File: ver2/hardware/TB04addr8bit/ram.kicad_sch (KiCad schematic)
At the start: 5 parts, among them U1 74AHC04, U34 6116, U35 74LS08, U36 74HC00

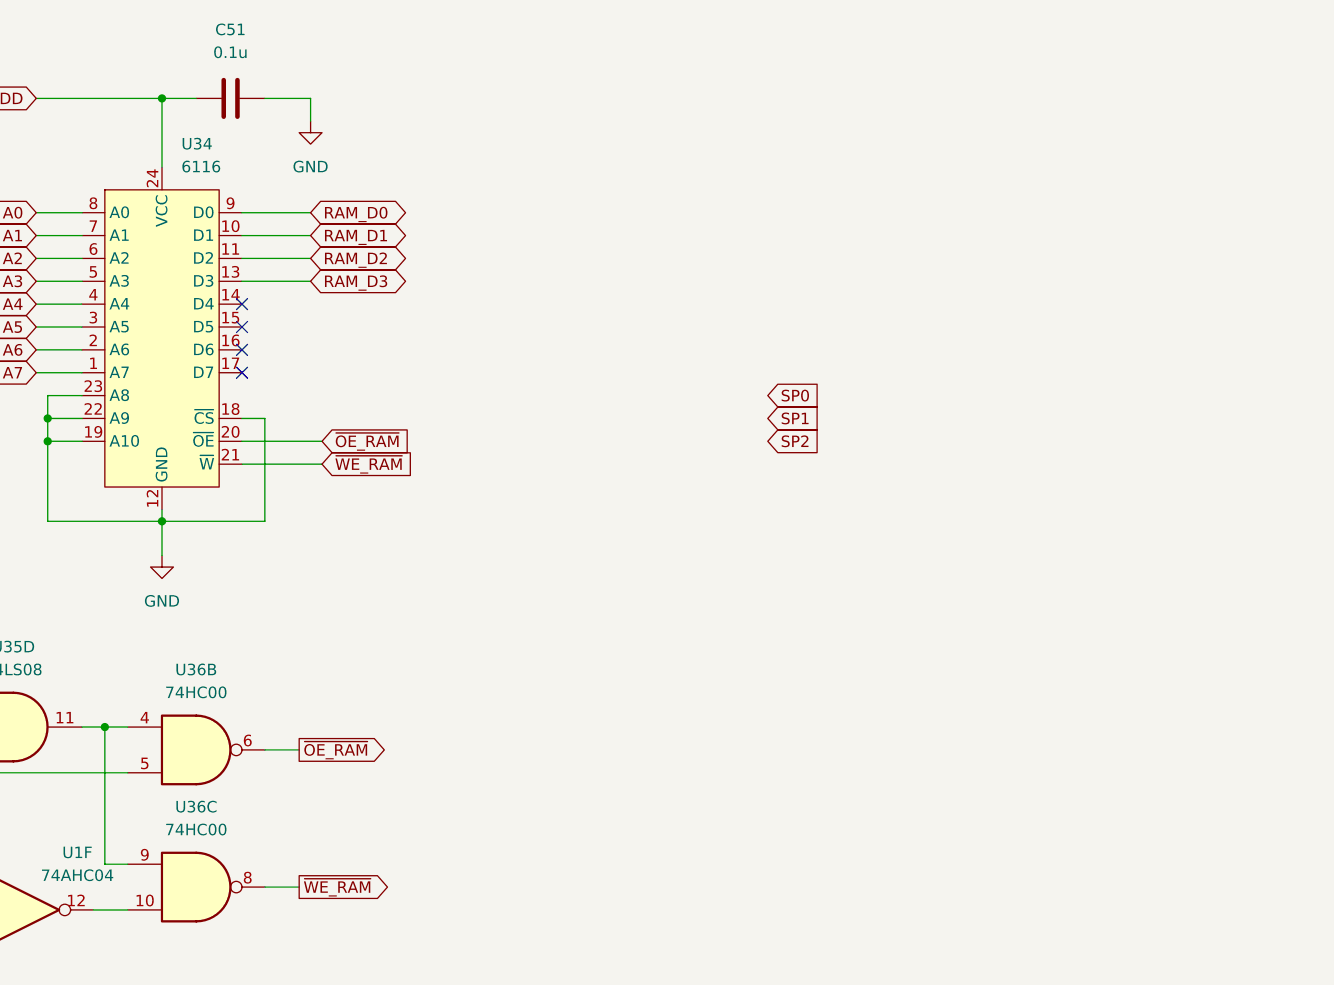
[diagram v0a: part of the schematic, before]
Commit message: ver2: 命令ラッチを1相ずらし、アドレスMUXを完成、I/Oと周辺ICを配置
- 命令ラッチの取り込みエッジを1相ずらし(U20 Cp=FCH1→FCH2 /
  U26 Cp=FCH2→DCR)。EXE中はアドレスバスがmAddrになるため、
  従来はEXE→FCH1の境目でROMのアクセスが間に合わなかった
- /OE_ROM のゲート入力を ~WE から ~WR へ付け替え
  (レジスタ書込許可ではなくメモリ書込で判定するのが正)
- PCの161出力をアドレスバスから切り離し、244経由に変更
  U42(PC)/U43(mAddr)/U44(SP)の入出力を結線し A0-A7 を駆動
  U44は 11110+SP[2:0] で 0xF0-0xF7 を生成。IN/OUT用の244は廃止
- PCのカウントイネーブルを 74LS32 の空きゲートで FCH1|FCH2 として生成
- PC_mAddr シートを PC へ改称し、分岐ロード用の 8bit 2:1 MUX
  (74LS157×2, U14/U15)を新設。出力 PC0-7 を161のD入力へ
  PCカウンタ(IC9/IC10)は addrMUX シートへ移動
- 6116 の /CS にゲートを追加(P2 & !P5)、D4-D7 にラベルを付与
- Yドライバ(74HC244×2, U16/U17)、inPort の 74LS253×2、
  outPort の 74HC273+LED4個 を配置(結線は未)
- ルートから未参照だった ROM_ALU_Decoder / interFace / RS02 を削除

未了: 共通8bitデータバス、オペランド源MUX(SEL_A/SEL_B/SEL_IMM/SEL_Y)、
I/Oポートの結線。PC_mAddr.kicad_sch は PC.kicad_sch と同一内容の
残骸として残っている

Co-Authored-By: Claude Opus 5 <noreply@anthropic.com>
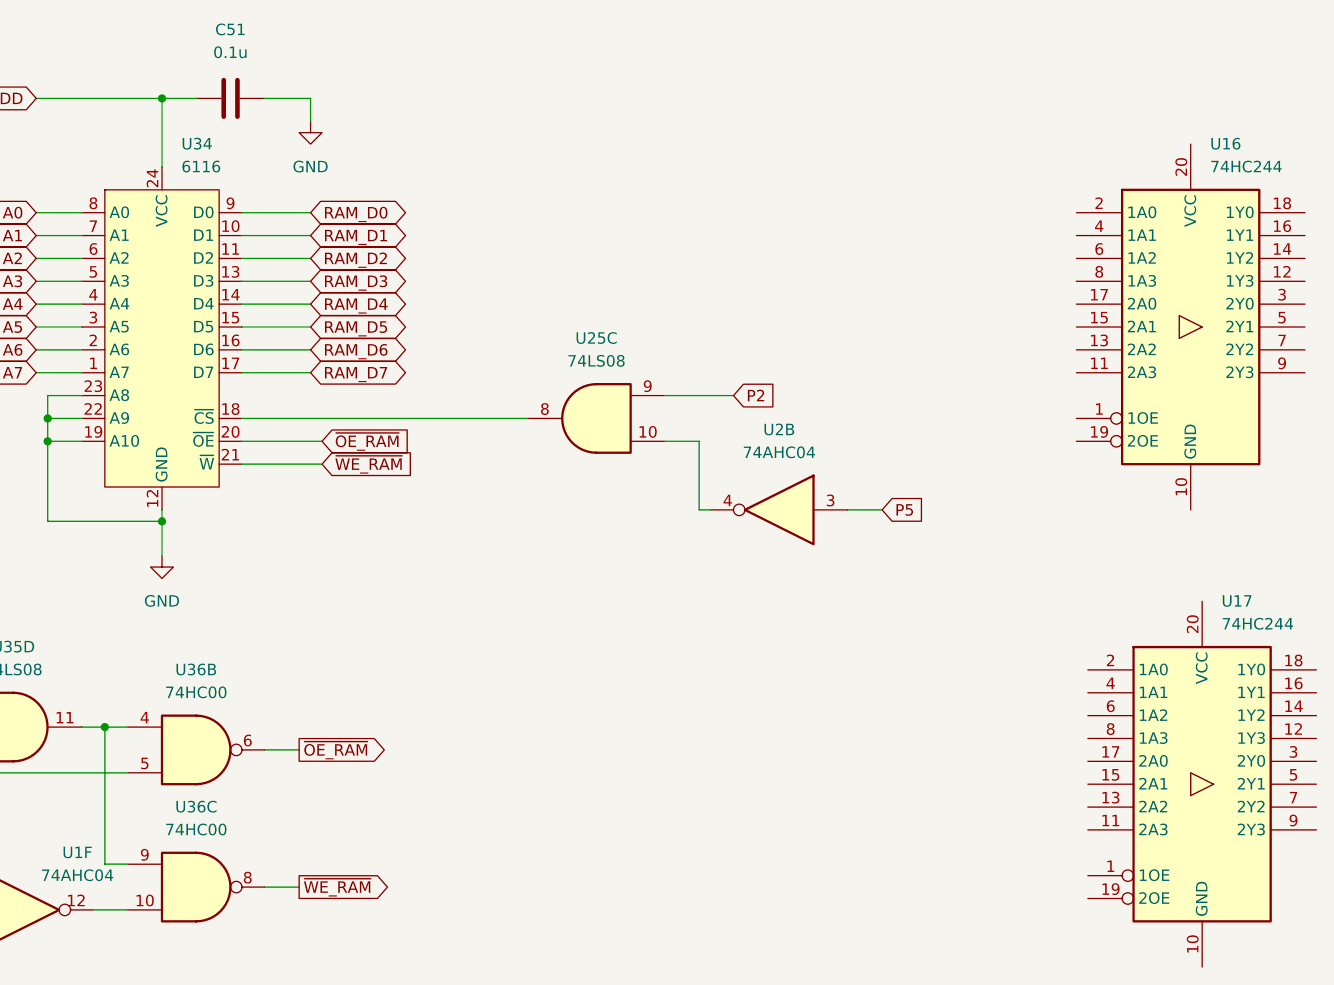
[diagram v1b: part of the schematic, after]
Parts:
- added U16, U17: 74HC244, symbol 74xx:74HC244
- added U2: 74AHC04, symbol 74xx:74AHC04
- added U25: 74LS08, symbol 74xx:74LS08
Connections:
- net GND: no longer U34.18 (~{CS})
- net RAM_D4: now reaches U34.14 (D4)
- net RAM_D5: now reaches U34.15 (D5)
- net RAM_D6: now reaches U34.16 (D6)
- net RAM_D7: now reaches U34.17 (D7)
- new net: U2.4, U25.10
- new net: U25.8, U34.18 (~{CS})
- new net P2: U25.9
- new net P5: U2.3
- no-connect marks 4 -> 0

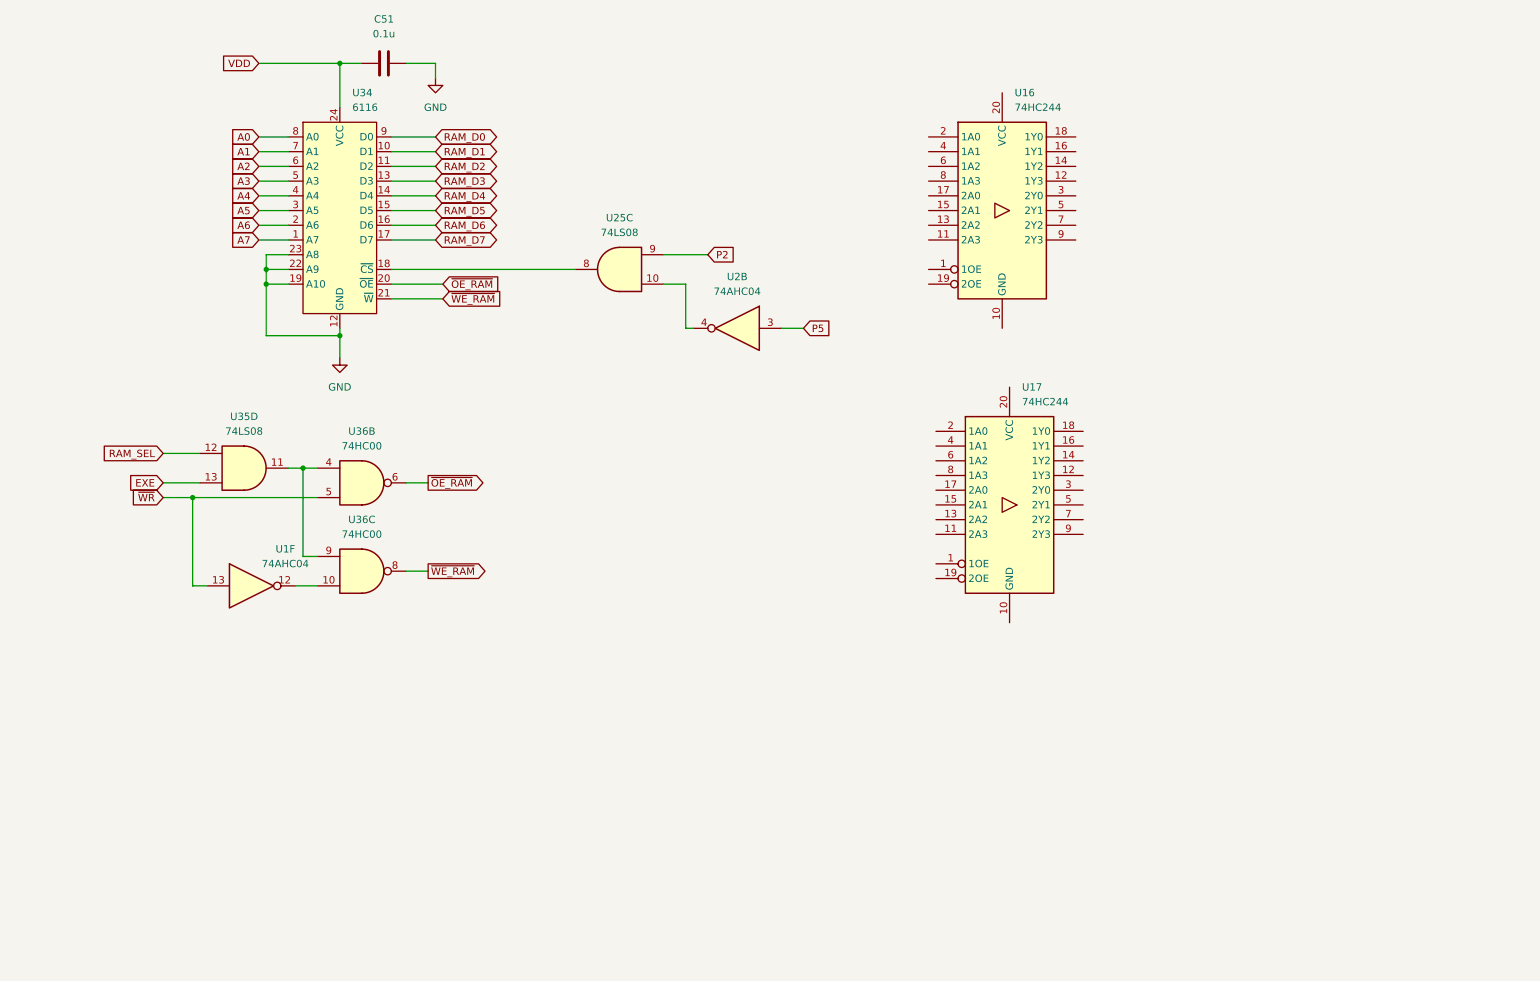
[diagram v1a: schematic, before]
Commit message: ver2: 要修正5件を修正し共通データバス・オペランド源MUX・I/Oを結線
- 6116の/CS極性を修正し、スタック域を含むRAM_STK_SEL(0xC0-0xF7)に統一
- ALU出力をDI0-3へ直結、U21はYドライバ源として残す(LD/POP/RET対策)
- 共通8bitデータバスMD0-7を新設(ROM/RAM/Yドライバ/IN244が排他駆動)
- aポートMUX(74LS253x2)・IN用244・Yドライバ制御ゲートを追加
- IN実行時のROM競合を/OE_ROMに~OE_iAddrを足して回避
- 4bit書込時にMD4-7が浮くのをU17 bank2で0駆動
- 74LS157のEをGND固定、孤立したPC_mAddrシートを削除

Co-Authored-By: Claude Opus 5 <noreply@anthropic.com>
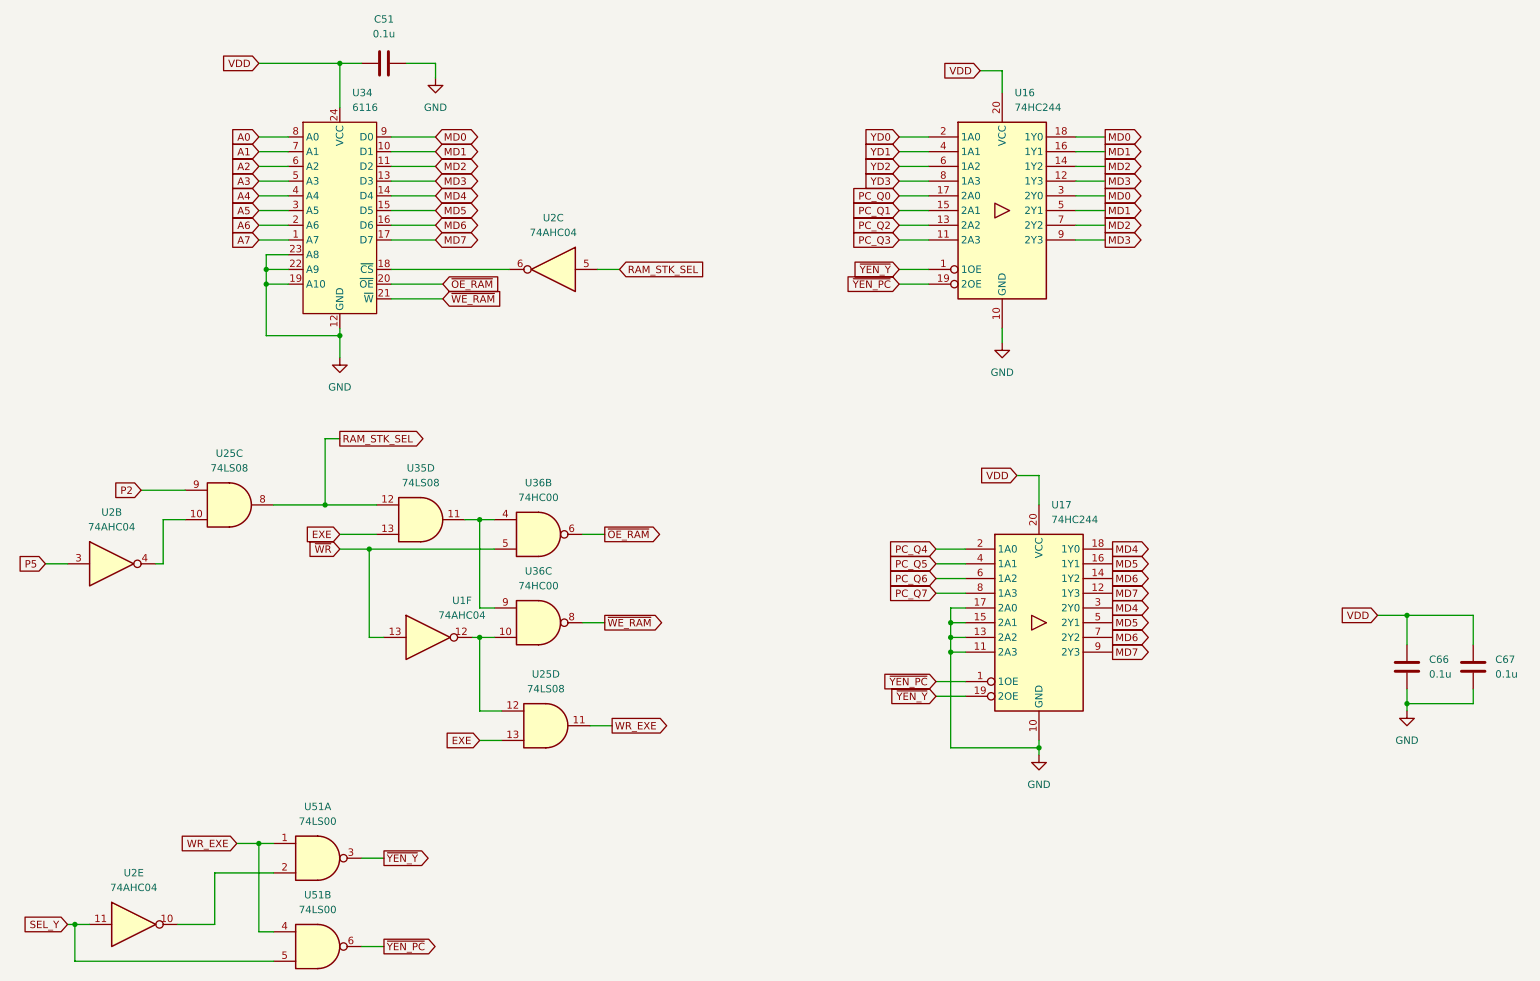
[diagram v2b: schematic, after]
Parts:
- added C66, C67: 0.1u, symbol Device:C
- added unit 3 of U2
- added unit 5 of U2
- added unit 4 of U25
- added U51: 74LS00, symbol 74xx:74LS00
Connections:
- net RAM_D0 is gone; now on net MD0: U34.9 (D0)
- net RAM_D1 is gone; now on net MD1: U34.10 (D1)
- net RAM_D2 is gone; now on net MD2: U34.11 (D2)
- net RAM_D3 is gone; now on net MD3: U34.13 (D3)
- net RAM_D4 is gone; now on net MD4: U34.14 (D4)
- net RAM_D5 is gone; now on net MD5: U34.15 (D5)
- net RAM_D6 is gone; now on net MD6: U34.16 (D6)
- net RAM_D7 is gone; now on net MD7: U34.17 (D7)
- net EXE: now also U25.13
- net GND: now also U16.10 (GND), U17.10 (GND), U17.11 (2A3), U17.13 (2A2), U17.15 (2A1), U17.17 (2A0), C66.1, C67.1
- net VDD: now also U16.20 (VCC), U17.20 (VCC), C66.2, C67.2
- net at U34.18 (~{CS}): now also U2.6; no longer U25.8
- net ~{YEN_PC}: now reaches U17.1 (1OE)
- net ~{YEN_PC}: now also U16.19 (2OE), U51.6
- net MD7: now reaches U17.12 (1Y3)
- net MD7: now also U17.9 (2Y3)
- net MD6: now reaches U17.14 (1Y2)
- net MD6: now also U17.7 (2Y2)
- net MD5: now reaches U17.16 (1Y1)
- net MD5: now also U17.5 (2Y1)
- net MD4: now reaches U17.18 (1Y0)
- net MD4: now also U17.3 (2Y0)
- net ~{YEN_Y}: now reaches U17.19 (2OE)
- net ~{YEN_Y}: now also U16.1 (1OE), U51.3
- net PC_Q4: now reaches U17.2 (1A0)
- net PC_Q5: now reaches U17.4 (1A1)
- net PC_Q6: now reaches U17.6 (1A2)
- net PC_Q7: now reaches U17.8 (1A3)
- net at U1.12, U36.10: now also U25.12
- net PC_Q3: now reaches U16.11 (2A3)
- net MD3: now reaches U16.12 (1Y3)
- net MD3: now also U16.9 (2Y3)
- net PC_Q2: now reaches U16.13 (2A2)
- net MD2: now reaches U16.14 (1Y2)
- net MD2: now also U16.7 (2Y2)
- net PC_Q1: now reaches U16.15 (2A1)
- net MD1: now reaches U16.16 (1Y1)
- net MD1: now also U16.5 (2Y1)
- net PC_Q0: now reaches U16.17 (2A0)
- net MD0: now reaches U16.18 (1Y0)
- net MD0: now also U16.3 (2Y0)
- net YD0: now reaches U16.2 (1A0)
- net YD1: now reaches U16.4 (1A1)
- net YD2: now reaches U16.6 (1A2)
- net YD3: now reaches U16.8 (1A3)
- net RAM_SEL renamed RAM_STK_SEL
- net RAM_STK_SEL: now also U25.8, U2.5
- new net: U2.10, U51.2
- new net SEL_Y: U2.11, U51.5
- new net WR_EXE: U25.11, U51.1, U51.4
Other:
- moved on the sheet: U17, U1F, U2B, U35D, U36B, U36C

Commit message: ver2: ゲートICをgatesシートへ集約しアノテーションを掛け直し
- 分散していた8パッケージ(U1/U2/U5/U25/U35/U36/U37/U51)をgatesシートへ集約
- シートをまたぐ11本をグローバルラベル化(~P4/~P5/~OUT_SEL/~CS_RAM/
  ~OE_ROM/CLK_C/CLK_Z/PC_CNT_EN/~PC_PE/~Ena_RS01/~Enb_RS01)
- U40のP2入力がROM_SELに吸着していたのを修正(RAM_SELが逆条件だった)
- !P5の重複インバータを解消、未使用ゲート入力7本をGNDへ
- ALU入力MUXをinPut→PC、PCカウンタをaddrMUX→PCへ移動
- 全体を再アノテーション(シート順採番)。旧→新の対応は電気的変化なしを確認

Co-Authored-By: Claude Opus 5 <noreply@anthropic.com>
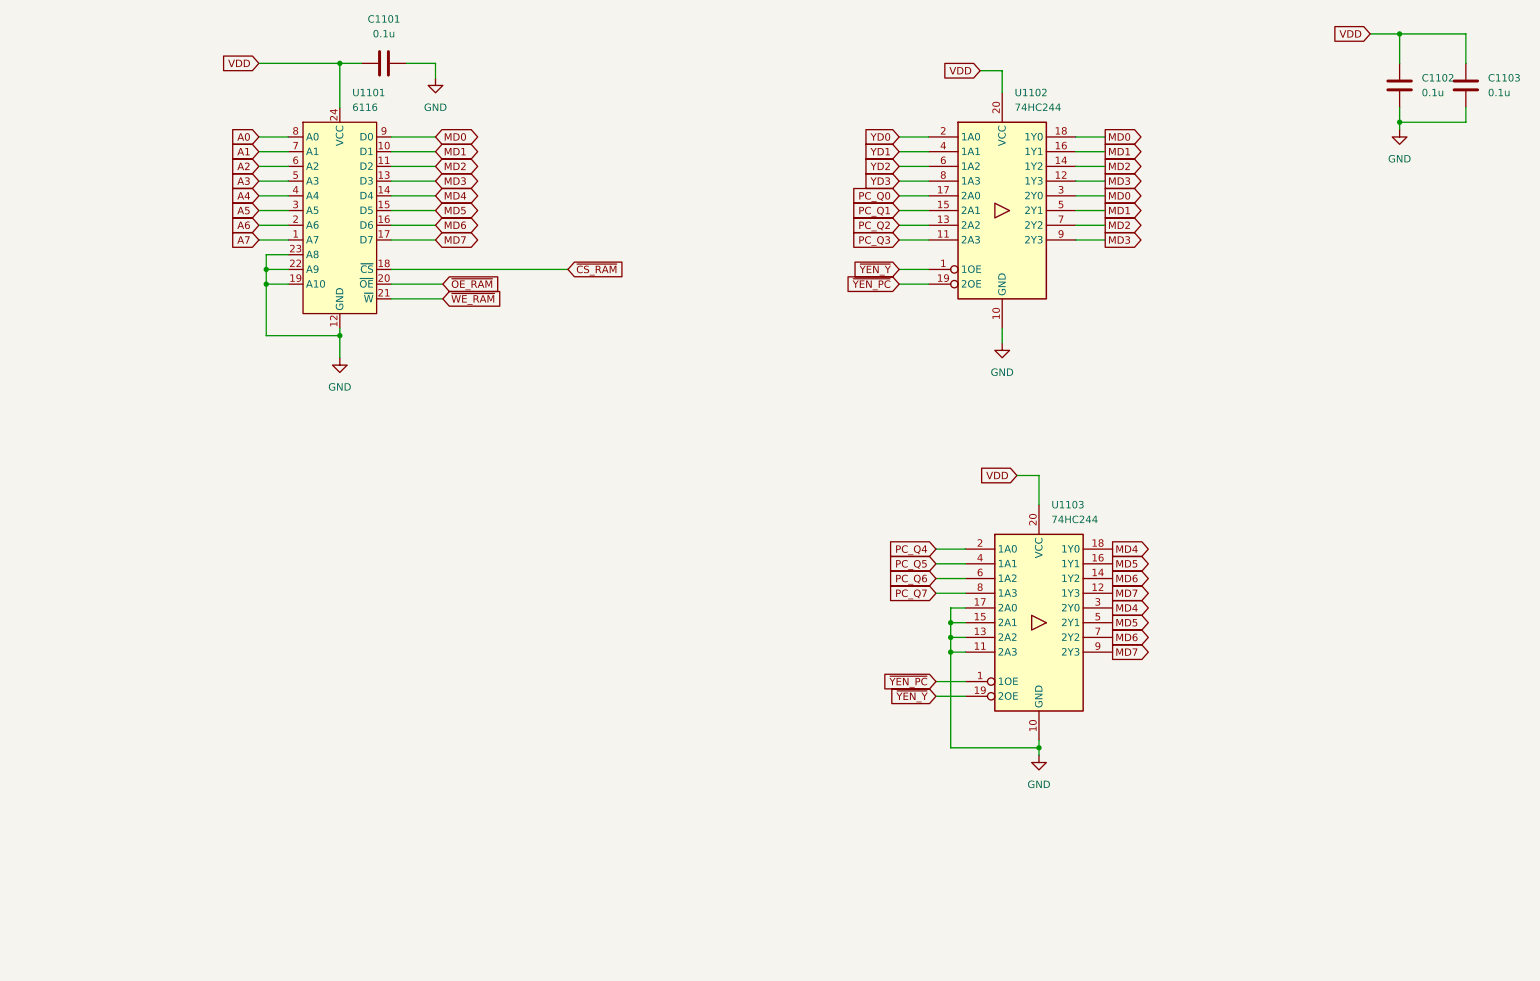
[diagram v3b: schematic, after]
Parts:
- removed U1, U2: 74AHC04, symbol 74xx:74AHC04
- removed U25, U35: 74LS08, symbol 74xx:74LS08
- removed U36: 74HC00, symbol 74xx:74HC00
- removed U51: 74LS00, symbol 74xx:74LS00
- renumbered C51 to C1101, C66 to C1102, C67 to C1103, U34 to U1101, U16 to U1102, U17 to U1103
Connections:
- net ~{CS_RAM}: now reaches U1101.18 (~{CS})
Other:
- moved on the sheet: C1102, C1103

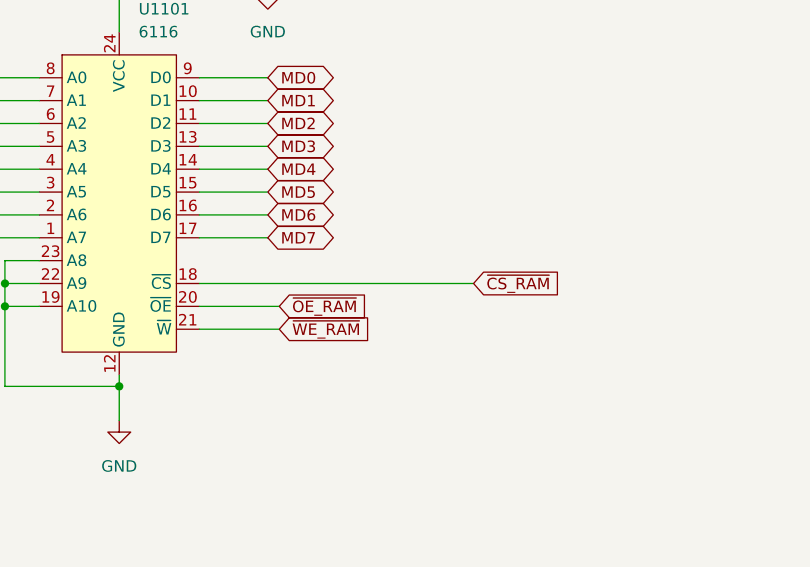
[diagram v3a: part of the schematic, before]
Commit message: ver2: 掃除とタイミング是正(ROMのEXEゲート・フラグクロックをFCH1へ)
- 消費先ゼロだったU1302(RAM_SEL/STACK_SEL/IN_SEL/P6)を削除し空きゲート入力をGNDへ
- /OE_ROMの条件を生の~WRから~WR_EXE(=!(WR&EXE))へ変更
  書込命令の次のフェッチでROMが閉じる問題を解消
- フラグDFFのクロックゲートをEXEからFCH1へ(CLK_C=FCH1&C_WE)
  INのZが間に合わない件と、Cin=C_prevの帰還でADD/SUBの結果が壊れる件を解消
- いずれもネットリストで接続変化を照合済み。ERCはエラー98(全てwire_dangling)・警告0

Co-Authored-By: Claude Opus 5 <noreply@anthropic.com>
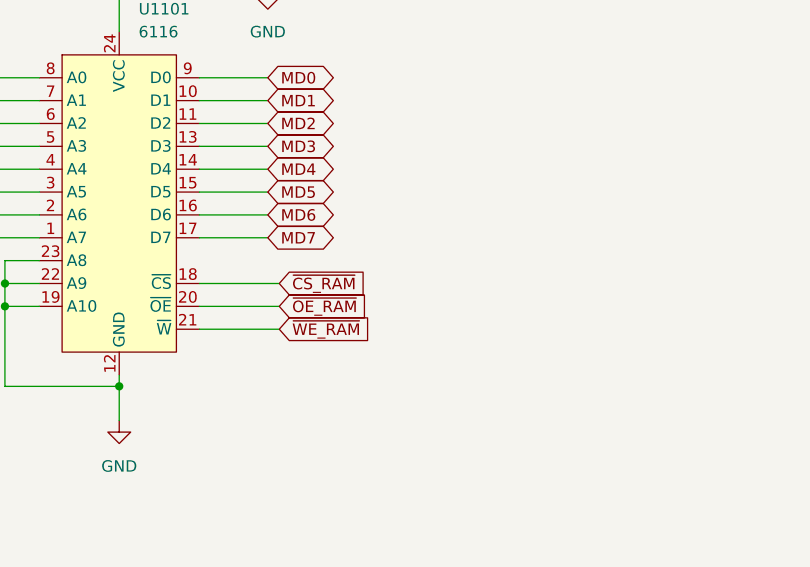
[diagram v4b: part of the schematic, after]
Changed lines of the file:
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@@
 	(wire
 		(pts
-			(xy 86.36 66.04) (xy 116.84 66.04)
+			(xy 86.36 66.04) (xy 95.25 66.04)
 		)
 		(stroke
@@
 	(global_label "~{CS_RAM}"
 		(shape input)
-		(at 116.84 66.04 0)
-		(fields_autoplaced yes)
-		(effects
-			(font
-				(size 1.27 1.27)
-			)
-			(justify left)
-		)
-		(property "Intersheetrefs" "${INTERSHEET_REFS}"
-			(at 127.0823 66.04 0)
-			(show_name no)
-			(do_not_autoplace no)
+		(at 95.25 66.04 0)
+		(fields_autoplaced yes)
+		(effects
+			(font
+				(size 1.27 1.27)
+			)
+			(justify left)
+		)
+		(property "Intersheetrefs" "${INTERSHEET_REFS}"
+			(at 105.4923 66.04 0)
+			(show_name no)
+			(do_not_autoplace no)
